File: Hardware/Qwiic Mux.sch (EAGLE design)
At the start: 78 parts, among them J1 SMD, J10 SMD, J11 PTH, J12 PTH, J13 PTH, J14 PTH, J2 SMD, J23 SMD, J24 SMD, J25 SMD, J26 SMD, J3 PTH, J4 PTH, J5 PTH, J6 PTH, J7 PTH, J8 SMD, J9 SMD, U2 PCA9548A, U3 3.3V/150mA, U4 2.8V/150mA

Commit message: Post design Review Changes
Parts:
- removed C10, C11, C13: 10uF, SparkFun-Capacitors:10UF-0603-6.3V-20%
- removed C12: 1.0uF, SparkFun-Capacitors:1.0UF-0603-16V-10%
- removed D1: GREEN, SparkFun-LED:LED-GREEN0603
- removed D4: BLUE, SparkFun-LED:LED-BLUE0603
- removed J11, J12, J13, J14, J3, J4, J5, J6, J7: PTH, SparkX:I2C_STANDARD_NO_SILK
- removed JP5: JUMPER-SMT_3_1-NC_TRACE_SILK, SparkFun-Jumpers:JUMPER-SMT_3_1-NC_TRACE_SILK
- removed R23, R25: 330, SparkFun-Resistors:330OHM-0603-1/10W-1%
- removed U3: 3.3V/150mA, SparkFun-IC-Power:V_REG_MIC52053.3V
- removed U4: 2.8V/150mA, SparkFun-IC-Power:V_REG_MIC52053.3V
- added FD3, FD4: FIDUCIAL1X2, SparkFun-Aesthetics:FIDUCIAL1X2
- added JP4: JUMPER-SMT_3_2-NC_PASTE_NO-SILK, SparkFun-Jumpers:JUMPER-SMT_3_2-NC_PASTE_NO-SILK
- D2: value Yellow -> RED; device SparkFun-LED:LED-YELLOW0603 -> SparkFun-LED:LED-RED0603
- R24: value 330 -> 1k; device SparkFun-Resistors:330OHM-0603-1/10W-1% -> SparkFun-Resistors:1KOHM-0603-1/10W-1%
- U2: device SparkX:TCA9548A -> SparkFun-IC-Logic:PCA9548A
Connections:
- removed net 2.8V: C13.1, C4.1, C7.1, D1.A, J12.VCC, J24.VCC, J6.VCC, J9.VCC, R10.1, R13.1, R14.1, R9.1, U4.OUT
- removed net 5V: C10.1, C5.1, C6.1, D4.A, J10.VCC, J11.VCC, J23.VCC, J7.VCC, JP5.1, R11.1, R12.1, R2.1, R3.1, U3.EN, U3.IN
- removed net N$4: D4.C, R23.2
- removed net VIN: J2.VCC, J3.VCC, JP5.2
- new net N$2: JP4.3, R4.1
- net 3.3V: now also C4.1, C5.1, C6.1, C7.1, J10.VCC, J2.VCC, J23.VCC, J24.VCC, J9.VCC, JP4.2, R10.1, R11.1, R12.1, R13.1, R14.1, R2.1, R3.1, R9.1; no longer C11.1, C12.1, J13.VCC, J14.VCC, J4.VCC, J5.VCC, JP5.3, R4.1, R5.1, U3.OUT, U4.EN, U4.IN
- net GND: no longer C10.2, C11.2, C12.2, C13.2, J11.GND, J12.GND, J13.GND, J14.GND, J3.GND, J4.GND, J5.GND, J6.GND, J7.GND, R23.1, R25.1, U3.GND, U4.GND
- net MAIN_SCL: no longer J3.SCL
- net MAIN_SDA: no longer J3.SDA
- net N$3: now also JP4.1, R5.1; no longer D1.C, R25.2
- net SCL0: no longer J4.SCL
- net SCL1: no longer J5.SCL
- net SCL2: no longer J6.SCL
- net SCL3: no longer J7.SCL
- net SCL4: no longer J11.SCL
- net SCL5: no longer J12.SCL
- net SCL6: no longer J13.SCL
- net SCL7: no longer J14.SCL
- net SDA0: no longer J4.SDA
- net SDA1: no longer J5.SDA
- net SDA2: no longer J6.SDA
- net SDA3: no longer J7.SDA
- net SDA4: no longer J11.SDA
- net SDA5: no longer J12.SDA
- net SDA6: no longer J13.SDA
- net SDA7: no longer J14.SDA
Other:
- note added: "Default 7-Bit I2C Address: 0x70 ADR lines can be set with below jumpers if multiple multiplexers are needed"
- note added: "I2C Multiplex"
- note added: "Qwiic Connectors"
- note added: "VIN: 3.3V - Range depends on sensors"
- note removed: "0: 3.3V Bus"
- note removed: "1: 3.3V Bus"
- note removed: "2: 2.8V Bus"
- note removed: "3: 5V Bus"
- note removed: "4: 5V Bus"
- note removed: "500mA"
- note removed: "5: 2.8V Bus"
- note removed: "6: 3.3V Bus"
- note removed: "7: 3.3V Bus"
- note removed: "By default 3.3V is provided by master"
- note removed: "Default 7-Bit I2C Address: 0x70 ADR lines can be set if multiple multiplexers are needed"
- note removed: "I2C Connectors"
- note removed: "Note: 5V bus only functional if 5V is provided by Vin"
- note removed: "Power"
- note removed: "Provide 5V in and move jumper to 5V to get regulated 3.3V output"
- note removed: "VIN: 3.3V default"
- moved on the sheet: C1, C2, C3, C4, C5, C6, C7, C8, C9, D2, J1, J10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

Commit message: checklist changes
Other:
- note added: "Clear jumper JP4 to remove I2C pullup resistors"
- note added: "v10"
- note removed: "v01"
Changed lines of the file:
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@@
 <?xml version="1.0" encoding="utf-8"?>
 <!DOCTYPE eagle SYSTEM "eagle.dtd">
-<eagle version="7.7.0">
+<eagle version="9.0.1">
 <drawing>
 <settings>
 <setting alwaysvectorfont="no"/>
+<setting keepoldvectorfont="yes"/>
 <setting verticaltext="up"/>
 </settings>
@@
 <plain>
 <text x="166.37" y="11.684" size="2.54" layer="94" font="vector">N. Seidle</text>
-<text x="236.22" y="7.62" size="2.032" layer="94" font="vector" ratio="10">v01</text>
+<text x="236.22" y="7.62" size="2.032" layer="94" font="vector" ratio="10">v10</text>
 <text x="71.12" y="132.08" size="3.048" layer="97" font="vector" ratio="12" align="center">Qwiic Connectors</text>
 <text x="195.58" y="111.76" size="1.778" layer="97" font="vector" align="center">Default 7-Bit I2C Address: 0x70
@@
 <wire x1="147.32" y1="35.56" x2="147.32" y2="185.42" width="0.1524" layer="97" style="longdash"/>
 <wire x1="149.86" y1="185.42" x2="147.32" y2="185.42" width="0.1524" layer="97" style="longdash"/>
+<text x="200.66" y="170.18" size="1.016" layer="97" font="vector">Clear jumper JP4 to
+remove I2C pullup resistors</text>
 </plain>
 <instances>

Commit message: Updated Qwiic connector
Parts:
- J1, J10, J23, J24, J25, J26, J8, J9: value SMD -> (none); device SparkX:I2C_STANDARDJS-1MM -> SparkFun-Connectors:QWIIC_CONNECTORJS-1MM
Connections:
- net 3.3V: now also J1.2, J10.2, J23.2, J24.2, J25.2, J26.2, J8.2, J9.2; no longer J1.VCC, J10.VCC, J23.VCC, J24.VCC, J25.VCC, J26.VCC, J8.VCC, J9.VCC
- net GND: now also J1.1, J10.1, J23.1, J24.1, J25.1, J26.1, J8.1, J9.1; no longer J1.GND, J10.GND, J23.GND, J24.GND, J25.GND, J26.GND, J8.GND, J9.GND
- net SCL0: now also J1.4; no longer J1.SCL
- net SCL1: now also J8.4; no longer J8.SCL
- net SCL2: now also J9.4; no longer J9.SCL
- net SCL3: now also J10.4; no longer J10.SCL
- net SCL4: now also J23.4; no longer J23.SCL
- net SCL5: now also J24.4; no longer J24.SCL
- net SCL6: now also J25.4; no longer J25.SCL
- net SCL7: now also J26.4; no longer J26.SCL
- net SDA0: now also J1.3; no longer J1.SDA
- net SDA1: now also J8.3; no longer J8.SDA
- net SDA2: now also J9.3; no longer J9.SDA
- net SDA3: now also J10.3; no longer J10.SDA
- net SDA4: now also J23.3; no longer J23.SDA
- net SDA5: now also J24.3; no longer J24.SDA
- net SDA6: now also J25.3; no longer J25.SDA
- net SDA7: now also J26.3; no longer J26.SDA

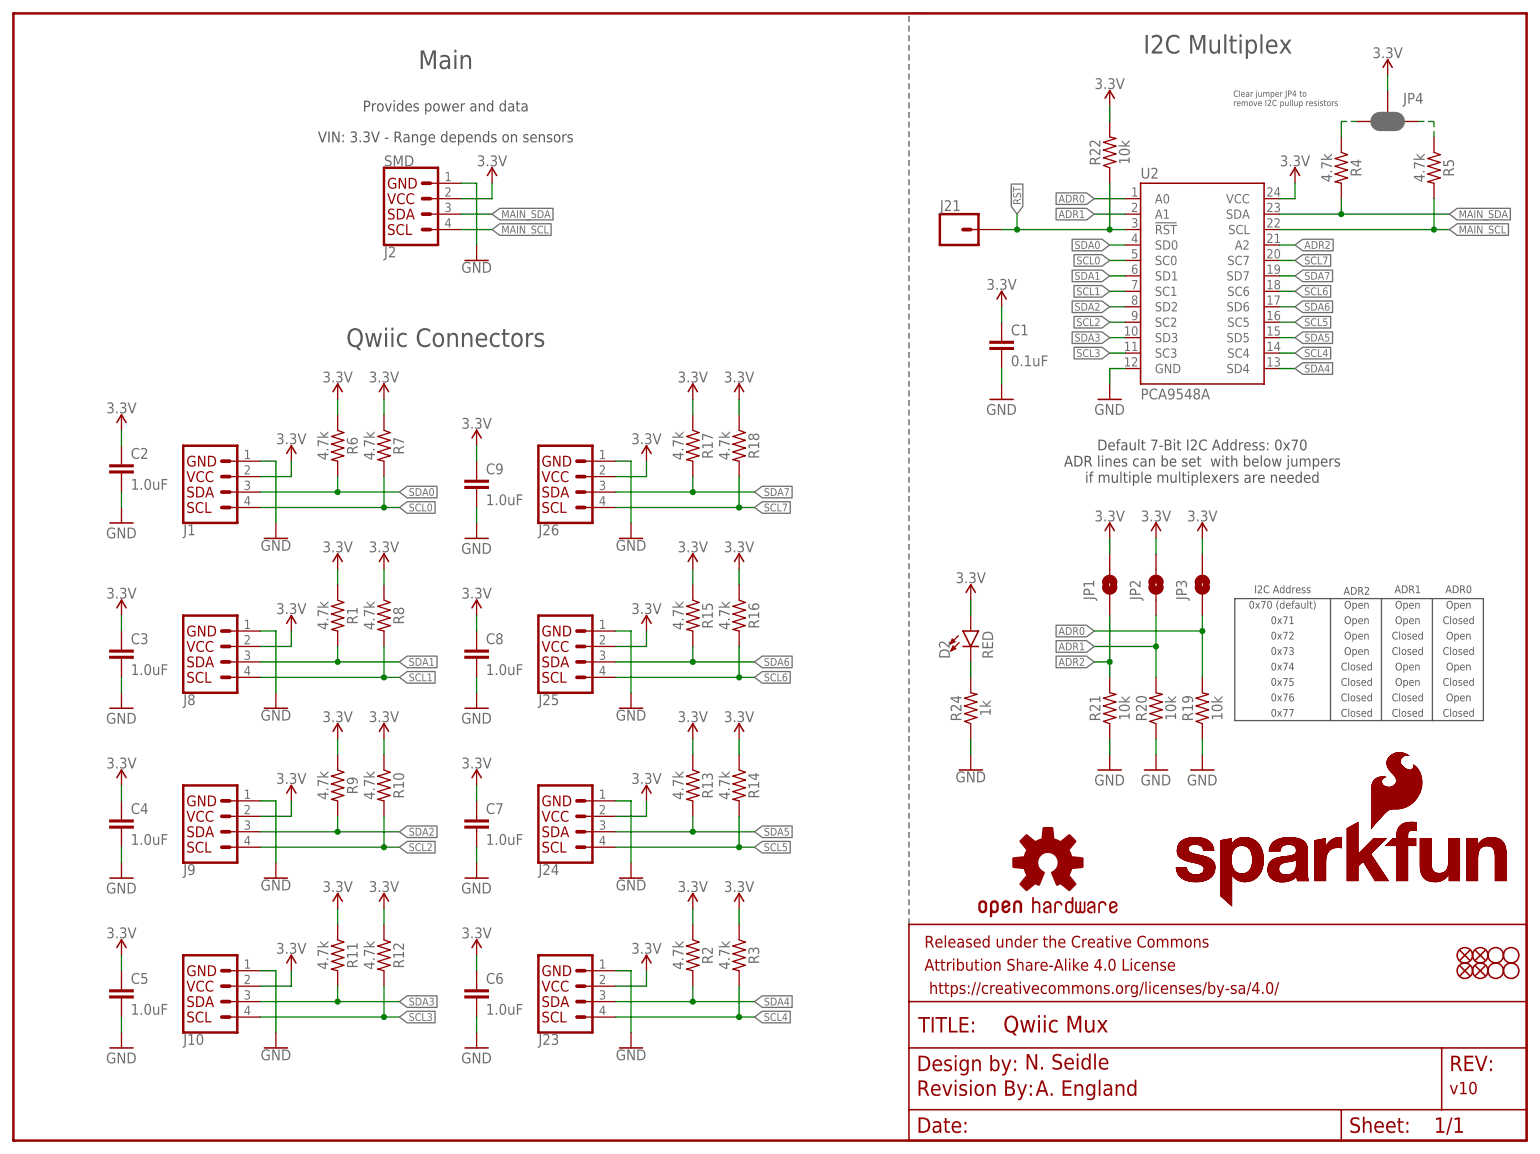
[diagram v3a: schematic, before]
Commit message: Update Board
Add second "Main" Qwiic connector
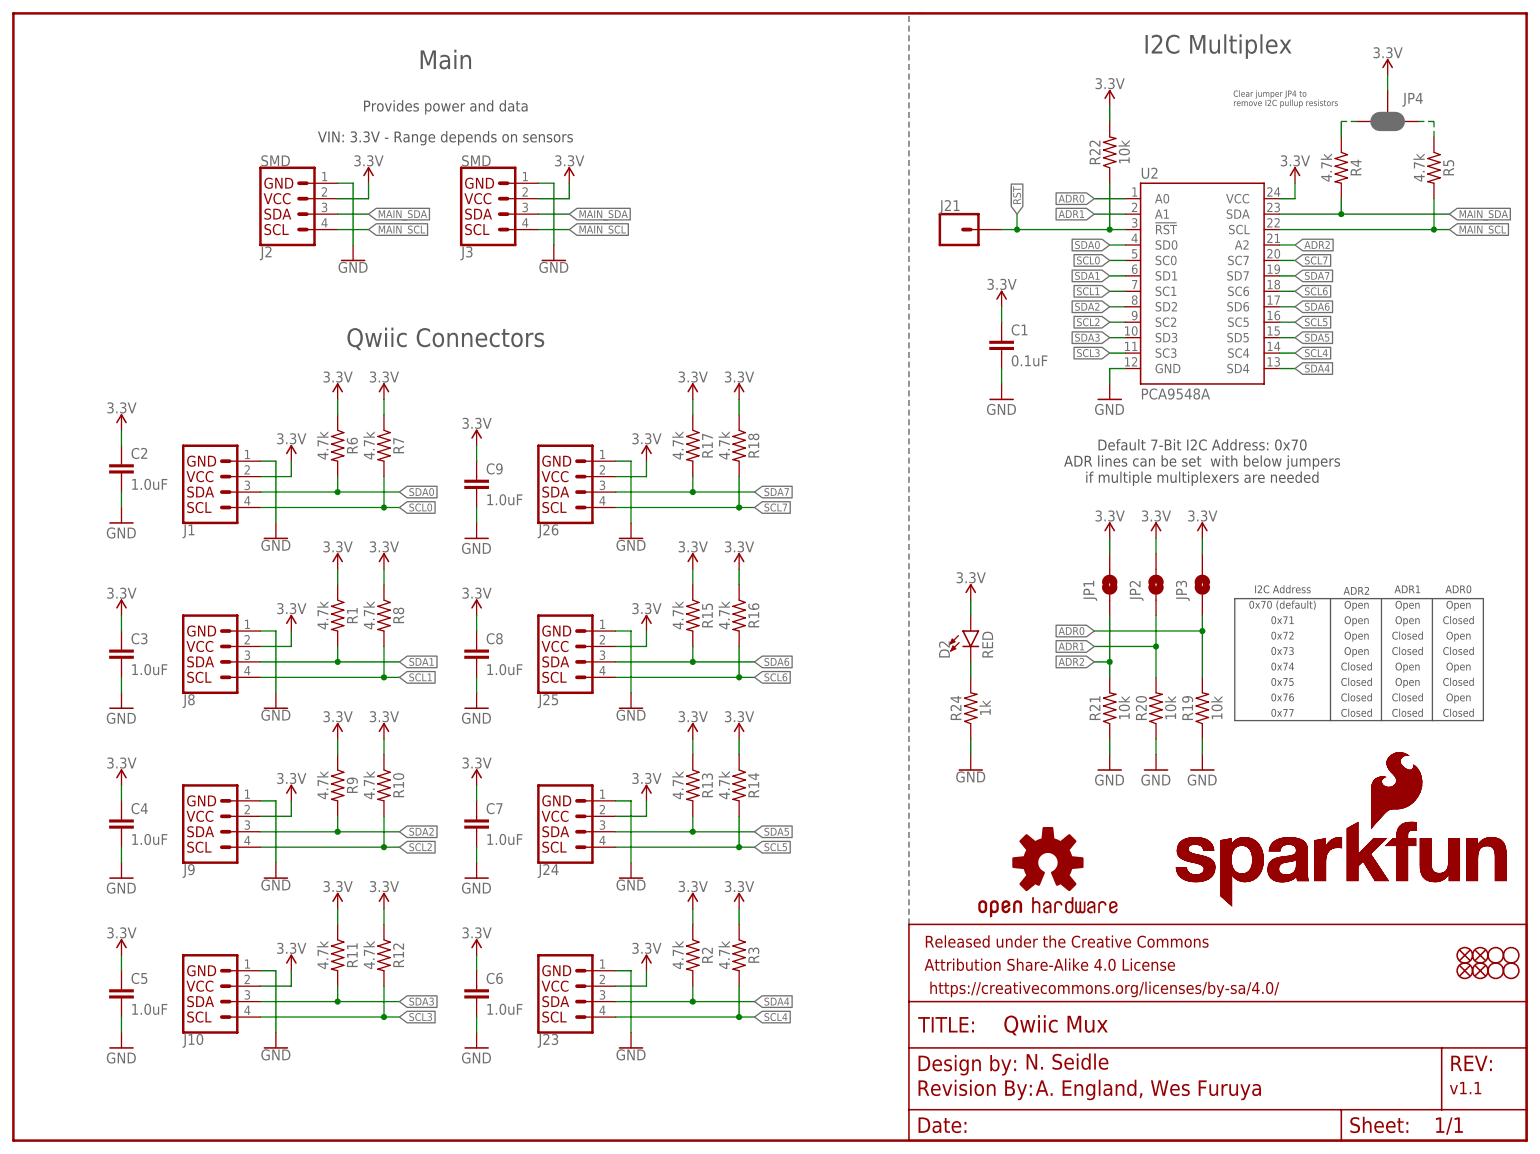
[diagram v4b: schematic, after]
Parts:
- added J3: SMD, SparkX:I2C_STANDARDJS-1MM
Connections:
- net 3.3V: now also J3.VCC
- net GND: now also J3.GND
- net MAIN_SCL: now also J3.SCL
- net MAIN_SDA: now also J3.SDA
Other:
- note added: "A. England, Wes Furuya"
- note added: "v1.1"
- note removed: "A. England"
- note removed: "v10"
- moved on the sheet: J2

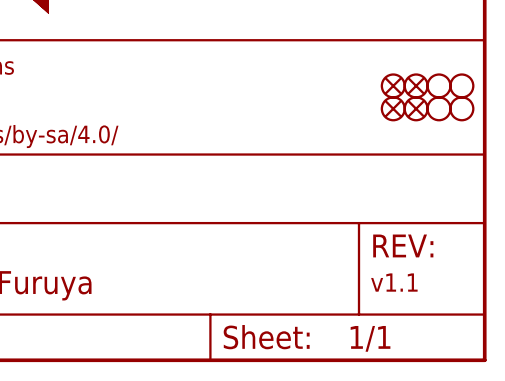
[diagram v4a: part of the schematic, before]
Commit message: Fix routing and version numbering
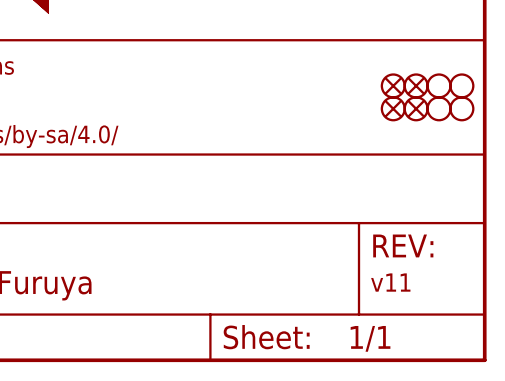
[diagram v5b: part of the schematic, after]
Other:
- note added: "v11"
- note removed: "v1.1"
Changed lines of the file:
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@@
 <plain>
 <text x="166.37" y="11.684" size="2.54" layer="94" font="vector">N. Seidle</text>
-<text x="236.22" y="7.62" size="2.032" layer="94" font="vector" ratio="10">v1.1</text>
+<text x="236.22" y="7.62" size="2.032" layer="94" font="vector" ratio="10">v11</text>
 <text x="71.12" y="132.08" size="3.048" layer="97" font="vector" ratio="12" align="center">Qwiic Connectors</text>
 <text x="195.58" y="111.76" size="1.778" layer="97" font="vector" align="center">Default 7-Bit I2C Address: 0x70
